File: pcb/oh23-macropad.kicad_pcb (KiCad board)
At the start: 2 copper layers, 67.2 x 29.1 mm, 9 parts, among them J1 Conn_01x11, SW1 SW_Push, SW2 SW_Push, SW3 SW_Push, U1 MOUDLE-SEEEDUINO-XIAO

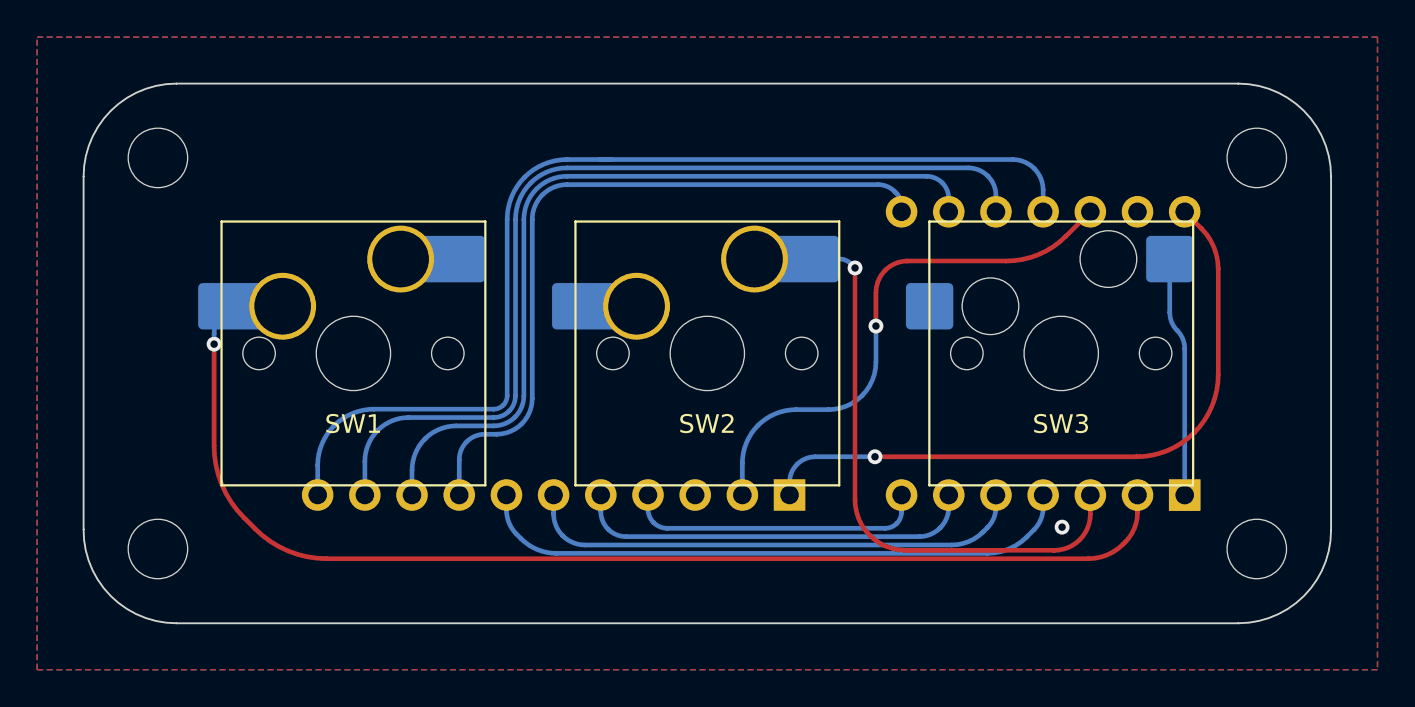
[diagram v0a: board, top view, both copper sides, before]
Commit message: Fix DRC, add order number location
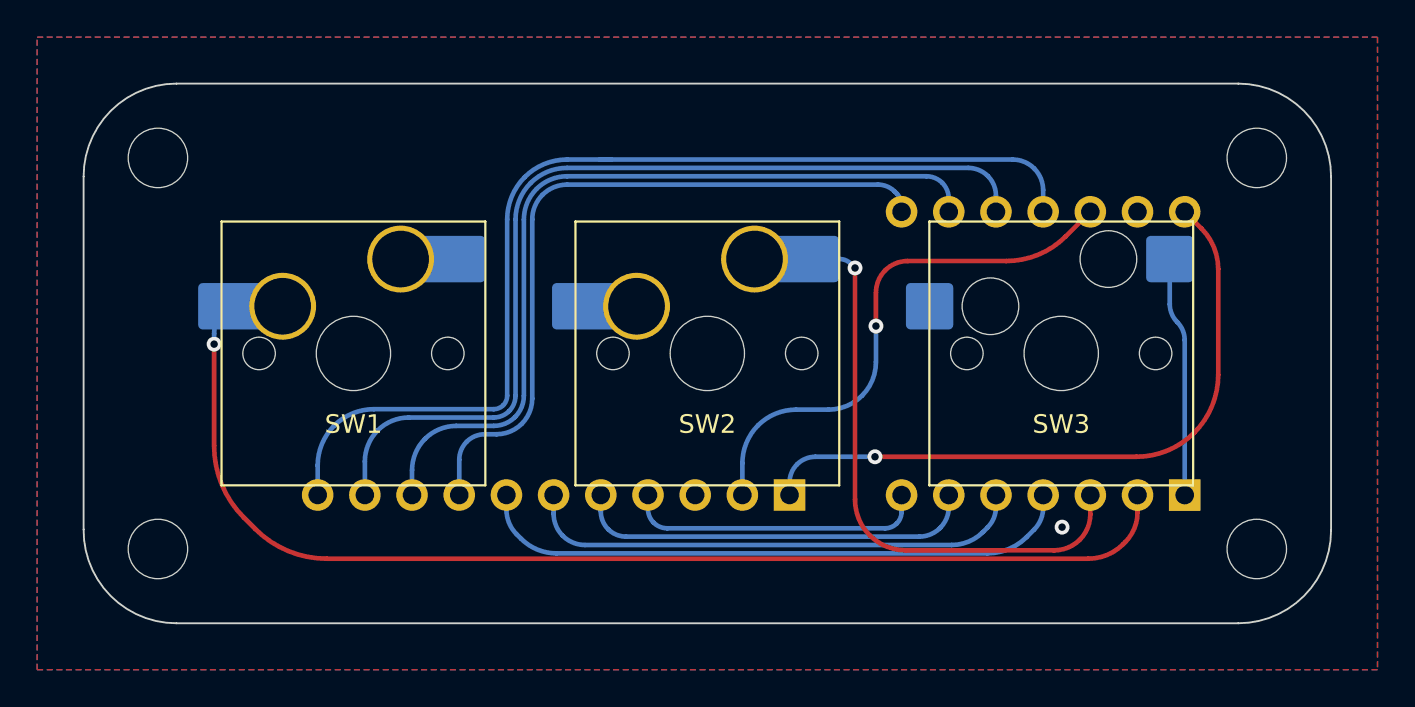
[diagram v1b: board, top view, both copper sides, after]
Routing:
- net Net-(SW3-Pad2): track 13.5 -> 12.9 mm
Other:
- board text added: "JLCJLCJLCJLC"
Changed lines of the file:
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@@
   (net 10 "/GP03_D10")
   (net 11 "Net-(SW2-Pad2)")
-  (net 12 "Net-(U1-Pad1)")
+  (net 12 "Net-(SW3-Pad2)")
   (net 13 "GND")
   (net 14 "Net-(SW1-Pad1)")
@@
       (net 13 "GND") (pinfunction "1") (pintype "passive"))
     (pad "2" smd roundrect locked (at 5.842 -5.08) (size 2.55 2.5) (layers "B.Cu" "B.Paste" "B.Mask") (roundrect_rratio 0.1)
-      (net 12 "Net-(U1-Pad1)") (pinfunction "2") (pintype "passive"))
+      (net 12 "Net-(SW3-Pad2)") (pinfunction "2") (pintype "passive"))
     (model "${KICAD6_3RD_PARTY}/3dmodels/com_github_perigoso_keyswitch-kicad-library/3d-library.3dshapes/SW_Hotswap_Kailh_MX.wrl"
       (offset (xyz 0 0 0))
@@
     (property "Sheetname" "")
     (attr smd)
-    (fp_text reference "U1" (at 0 -2.54 90) (layer "B.SilkS")
+    (fp_text reference "U1" (at -2.2 -2.38095) (layer "B.SilkS")
       (effects (font (size 0.889 0.889) (thickness 0.1016)) (justify mirror))
     )
@@
       (effects (font (size 0.6096 0.6096) (thickness 0.0762)) (justify mirror))
     )
-    (fp_text user "XIAO" (at -5 -2.625 unlocked) (layer "B.SilkS")
+    (fp_text user "XIAO" (at -5.2 -2.38095 unlocked) (layer "B.SilkS")
       (effects (font (size 1 1) (thickness 0.15)) (justify mirror))
     )
-    (fp_text user "Seeed Studio" (at -3.5 -2.625 unlocked) (layer "B.SilkS")
+    (fp_text user "Seeed Studio" (at -3.7 -2.38095 unlocked) (layer "B.SilkS")
       (effects (font (size 1 1) (thickness 0.15)) (justify mirror))
     )
@@
     (fp_line (start 8.557768 -9.586087) (end 8.584184 -9.544686) (layer "B.Fab") (width 0.0254))
     (pad "1" thru_hole rect (at -7.625 7.62 90) (size 1.7 1.7) (drill 1) (layers *.Cu *.Mask)
-      (net 12 "Net-(U1-Pad1)") (pinfunction "GP26_D00_A0") (pintype "unspecified"))
+      (net 12 "Net-(SW3-Pad2)") (pinfunction "GP26_D00_A0") (pintype "unspecified"))
     (pad "2" thru_hole circle (at -7.625 5.08 90) (size 1.7 1.7) (drill 1) (layers *.Cu *.Mask)
       (net 14 "Net-(SW1-Pad1)") (pinfunction "GP27_D01_A1") (pintype "unspecified"))
@@
     (effects (font (size 1 1) (thickness 0.15)) (justify left mirror))
   )
+  (gr_text "JLCJLCJLCJLC" (at 126.395 92.7 -90) (layer "B.SilkS")
+    (effects (font (size 0.8 0.8) (thickness 0.15)) (justify mirror))
+  )
   (gr_text "SPI_0" (at 81.785 103.7) (layer "B.SilkS")
     (effects (font (size 1 1) (thickness 0.15)) (justify mirror))
@@
   (arc (start 103.781429 98.718571) (mid 104.23161 98.417769) (end 104.762635 98.312142) (width 0.25) (layer "B.Cu") (net 1))
   (segment (start 118.240611 86.450338) (end 119.56595 85.125) (width 0.25) (layer "F.Cu") (net 2))
-  (segment (start 115.040961 87.775677) (end 109.733056 87.775677) (width 0.25) (layer "F.Cu") (net 2))
+  (segment (start 109.733056 87.775677) (end 115.040961 87.775677) (width 0.25) (layer "F.Cu") (net 2))
   (segment (start 108.02595 89.482783) (end 108.02595 91.275677) (width 0.25) (layer "F.Cu") (net 2))
   (via (at 108.02595 91.275677) (size 0.8) (drill 0.4) (layers "F.Cu" "B.Cu") (net 2))
   (arc (start 108.52595 88.275677) (mid 108.155895 88.829502) (end 108.02595 89.482783) (width 0.25) (layer "F.Cu") (net 2))
-  (arc (start 109.733056 87.775677) (mid 109.079775 87.905622) (end 108.52595 88.275677) (width 0.25) (layer "F.Cu") (net 2))
+  (arc (start 108.52595 88.275677) (mid 109.079775 87.905622) (end 109.733056 87.775677) (width 0.25) (layer "F.Cu") (net 2))
   (arc (start 118.240611 86.450338) (mid 116.772599 87.431232) (end 115.040961 87.775677) (width 0.25) (layer "F.Cu") (net 2))
-  (segment (start 108.02595 93.215016) (end 108.02595 91.275677) (width 0.25) (layer "B.Cu") (net 2))
+  (segment (start 108.02595 91.275677) (end 108.02595 93.215016) (width 0.25) (layer "B.Cu") (net 2))
   (segment (start 100.835 98.662309) (end 100.835 100.37) (width 0.25) (layer "B.Cu") (net 2))
   (segment (start 103.721632 95.775677) (end 105.465289 95.775677) (width 0.25) (layer "B.Cu") (net 2))
@@
   (segment (start 113.787717 102.363909) (end 114.029626 102.121999) (width 0.25) (layer "B.Cu") (net 4))
   (segment (start 90.675 101.376985) (end 90.675 100.37) (width 0.25) (layer "B.Cu") (net 4))
-  (segment (start 112.102035 103.062142) (end 92.360156 103.062142) (width 0.25) (layer "B.Cu") (net 4))
+  (segment (start 92.360156 103.062142) (end 112.102035 103.062142) (width 0.25) (layer "B.Cu") (net 4))
   (arc (start 113.787717 102.363909) (mid 113.014319 102.880677) (end 112.102035 103.062142) (width 0.25) (layer "B.Cu") (net 4))
   (arc (start 91.168571 102.568571) (mid 91.715275 102.933867) (end 92.360156 103.062142) (width 0.25) (layer "B.Cu") (net 4))
@@
   (segment (start 93.215 101.251335) (end 93.215 100.37) (width 0.25) (layer "B.Cu") (net 5))
   (arc (start 93.613571 102.213571) (mid 93.318585 101.772093) (end 93.215 101.251335) (width 0.25) (layer "B.Cu") (net 5))
-  (arc (start 110.352306 102.612142) (mid 110.962167 102.490832) (end 111.479182 102.145374) (width 0.25) (layer "B.Cu") (net 5))
+  (arc (start 111.479182 102.145374) (mid 110.962167 102.490832) (end 110.352306 102.612142) (width 0.25) (layer "B.Cu") (net 5))
   (arc (start 111.485055 102.139501) (mid 111.826167 101.628991) (end 111.94595 101.026803) (width 0.25) (layer "B.Cu") (net 5))
   (arc (start 93.613571 102.213571) (mid 94.055048 102.508556) (end 94.575806 102.612142) (width 0.25) (layer "B.Cu") (net 5))
@@
   (segment (start 88.625 95.024479) (end 88.625 85.539959) (width 0.25) (layer "B.Cu") (net 9))
   (segment (start 80.515 98.564342) (end 80.515 100.37) (width 0.25) (layer "B.Cu") (net 9))
-  (arc (start 114.48595 84.253359) (mid 114.372437 83.682695) (end 114.049182 83.198909) (width 0.25) (layer "B.Cu") (net 9))
+  (arc (start 114.049182 83.198909) (mid 114.372437 83.682695) (end 114.48595 84.253359) (width 0.25) (layer "B.Cu") (net 9))
   (arc (start 89.438604 83.575746) (mid 90.339792 82.97359) (end 91.402817 82.762142) (width 0.25) (layer "B.Cu") (net 9))
   (arc (start 112.994732 82.762142) (mid 113.565396 82.875654) (end 114.049182 83.198909) (width 0.25) (layer "B.Cu") (net 9))
@@
   (segment (start 106.080588 87.67) (end 104.27 87.67) (width 0.25) (layer "B.Cu") (net 11))
   (arc (start 106.66 87.91) (mid 106.394163 87.732373) (end 106.080588 87.67) (width 0.25) (layer "B.Cu") (net 11))
-  (segment (start 123.842 90.548248) (end 123.842 87.67) (width 0.25) (layer "B.Cu") (net 12))
-  (segment (start 124.64595 92.489155) (end 124.64595 100.375) (width 0.25) (layer "B.Cu") (net 12))
-  (arc (start 124.470617 87.67) (mid 124.230055 87.830738) (end 124.2865 88.1145) (width 0.25) (layer "B.Cu") (net 12))
-  (arc (start 124.243975 91.518702) (mid 124.54148 91.963949) (end 124.64595 92.489155) (width 0.25) (layer "B.Cu") (net 12))
-  (arc (start 124.243975 91.518702) (mid 123.946469 91.073454) (end 123.842 90.548248) (width 0.25) (layer "B.Cu") (net 12))
+  (segment (start 124.64595 92.033663) (end 124.64595 100.375) (width 0.25) (layer "B.Cu") (net 12))
+  (segment (start 123.842 90.092756) (end 123.842 87.67) (width 0.25) (layer "B.Cu") (net 12))
+  (arc (start 124.243975 91.06321) (mid 124.54148 91.508457) (end 124.64595 92.033663) (width 0.25) (layer "B.Cu") (net 12))
+  (arc (start 123.842 90.092756) (mid 123.946469 90.617962) (end 124.243975 91.06321) (width 0.25) (layer "B.Cu") (net 12))
   (via (at 118.045 102.1) (size 0.8) (drill 0.4) (layers "F.Cu" "B.Cu") (free) (net 13))
   (segment (start 121.328788 103.022838) (end 121.444565 102.90706) (width 0.25) (layer "F.Cu") (net 14))
